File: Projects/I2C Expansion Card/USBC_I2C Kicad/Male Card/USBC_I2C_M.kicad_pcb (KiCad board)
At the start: 2 copper layers, 26 x 30 mm, 11 parts, among them U1 MCP2221AxSL

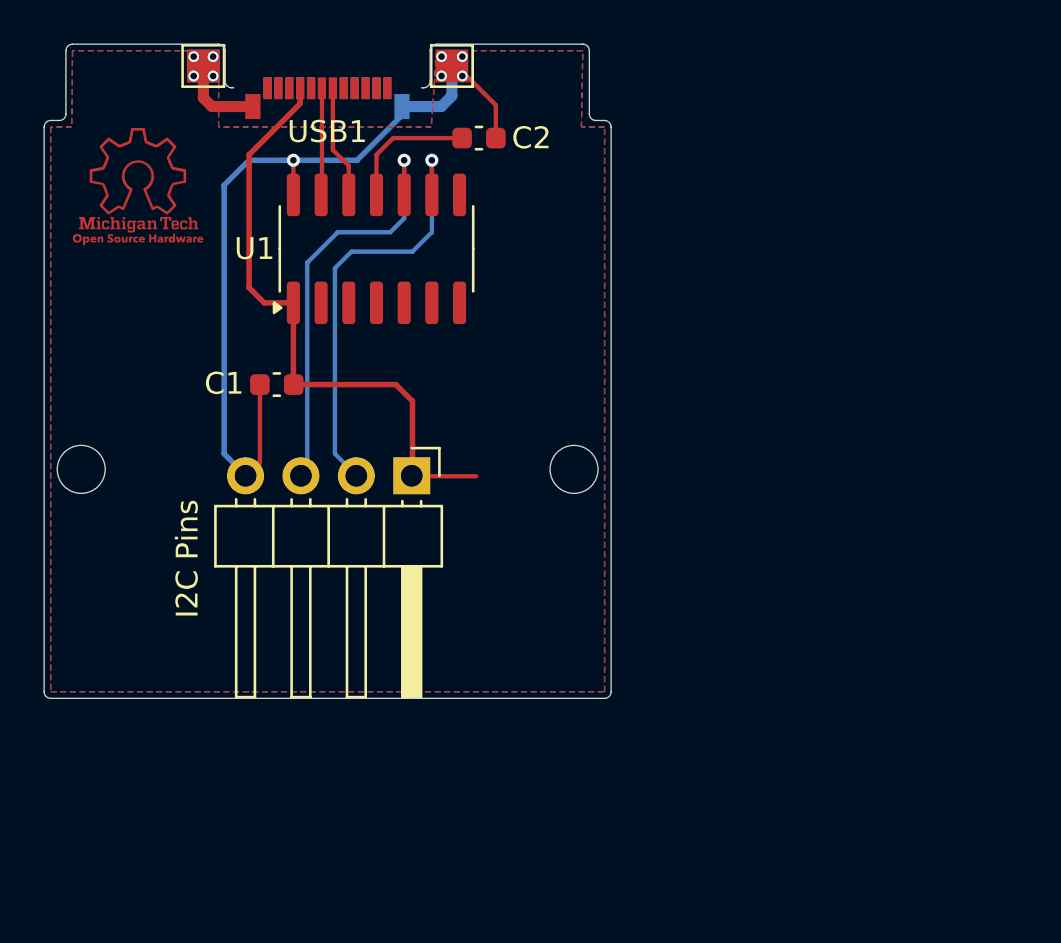
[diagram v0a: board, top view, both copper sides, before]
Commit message: Added Impedance Matching and added 5V Plane
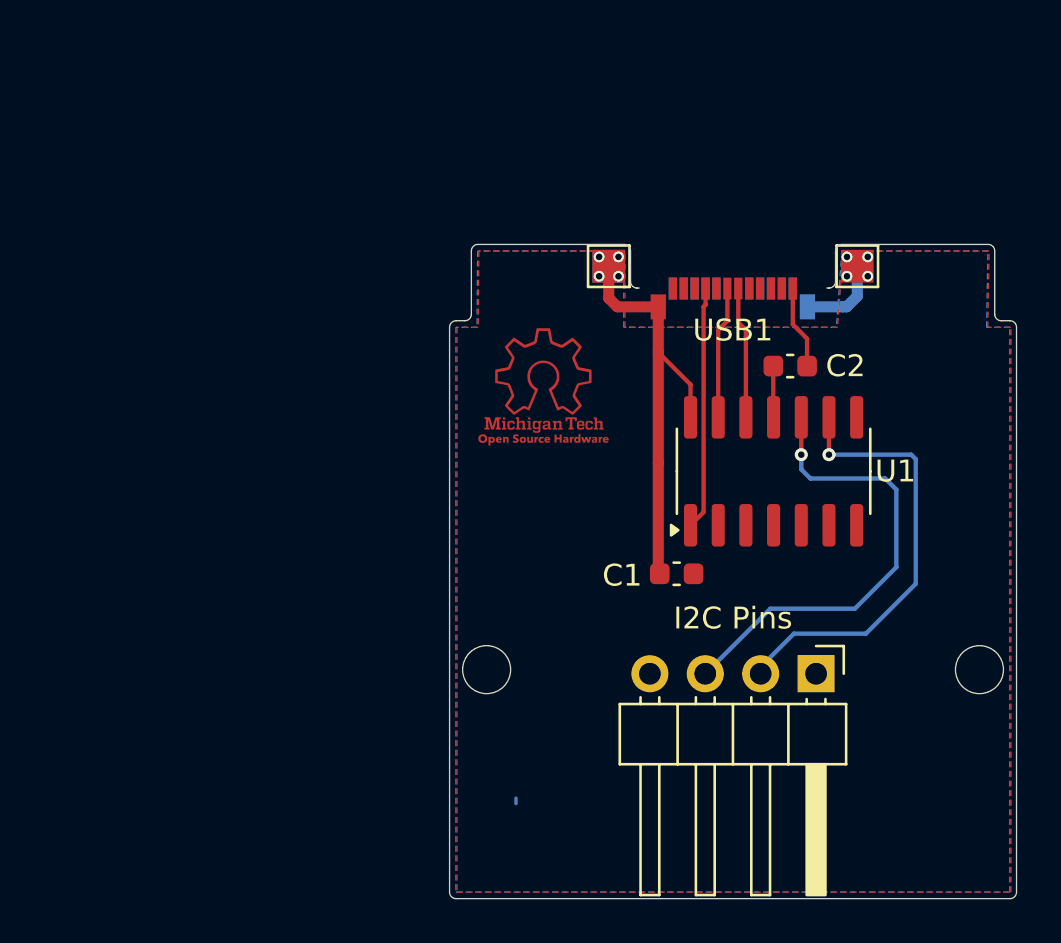
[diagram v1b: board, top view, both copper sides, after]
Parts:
- moved U1 20.9 mm to (114.8, 76.2)
- moved G*** 20.7 mm to (104.2, 72.4)
- moved H2 20.7 mm to (124.2, 85.3)
- moved TP1 20.7 mm to (107.2, 66.8)
- moved TP2 20.7 mm to (107.2, 66.8)
- moved H1 20.7 mm to (101.6, 85.3)
- moved TP3 20.7 mm to (118.6, 66.8)
- moved USB1 20.7 mm to (112.9, 67.8)
- moved I2C Pins 20.6 mm to (116.7, 85.5)
- moved C1 20.3 mm to (110.3, 80.9), turned to 180 degrees
- moved C2 17.7 mm to (115.5, 71.4)
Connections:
- C1 pad 1: GND -> 5V
- C1 pad 2: 5V -> GND
- I2C Pins pad 1: (no net) -> 5V
- I2C Pins pad 2: (no net) -> SDA
- I2C Pins pad 3: (no net) -> SCL
- I2C Pins pad 4: (no net) -> GND
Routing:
- net 5V: track 28.1 -> 11.1 mm
- net GND: track 41.9 -> 27.9 mm, vias 9 -> 8
- net Net-(U1-VUSB): track 6.08 -> 2.36 mm
- net SCL: track 19.4 -> 21.8 mm
- net Net-(U1-D+): track 4.91 -> 6.08 mm
- net Net-(U1-D-): track 5.19 -> 6.05 mm
- net SDA: track 20.0 -> 20.5 mm
- added copper zone on F.Cu, net 5V
- removed copper zone on F.Cu, net GND
